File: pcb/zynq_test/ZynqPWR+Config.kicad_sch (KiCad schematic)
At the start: 1 part, among them U1 XC7Z020-2CLG400I

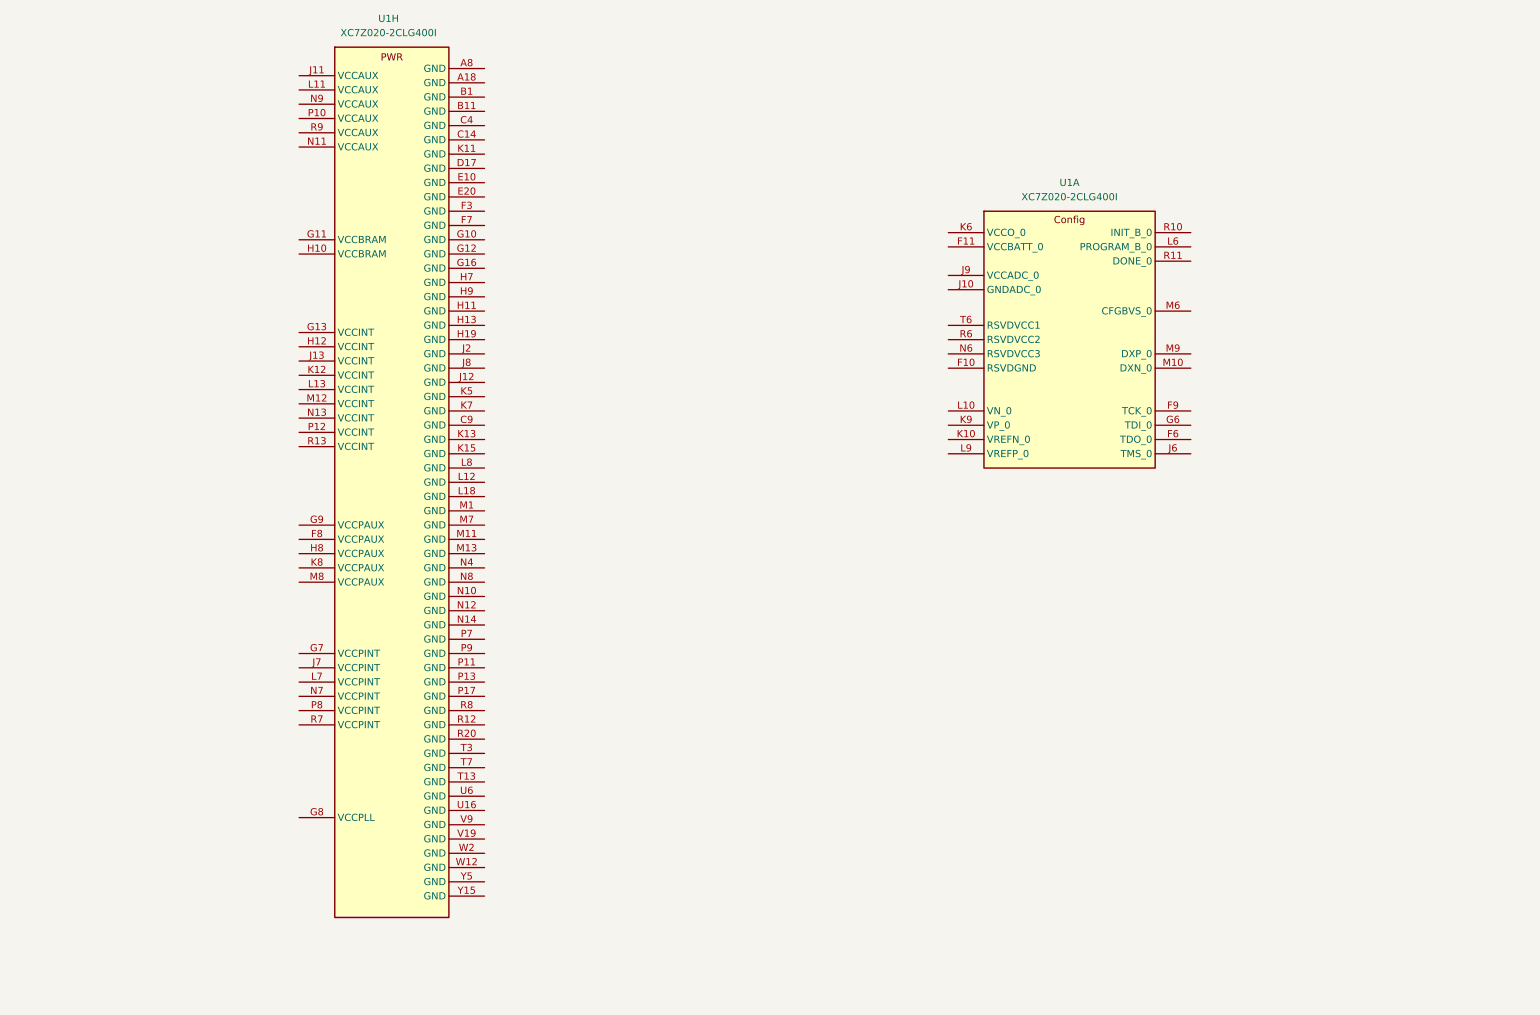
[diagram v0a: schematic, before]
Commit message: Finished PS, started on PWR
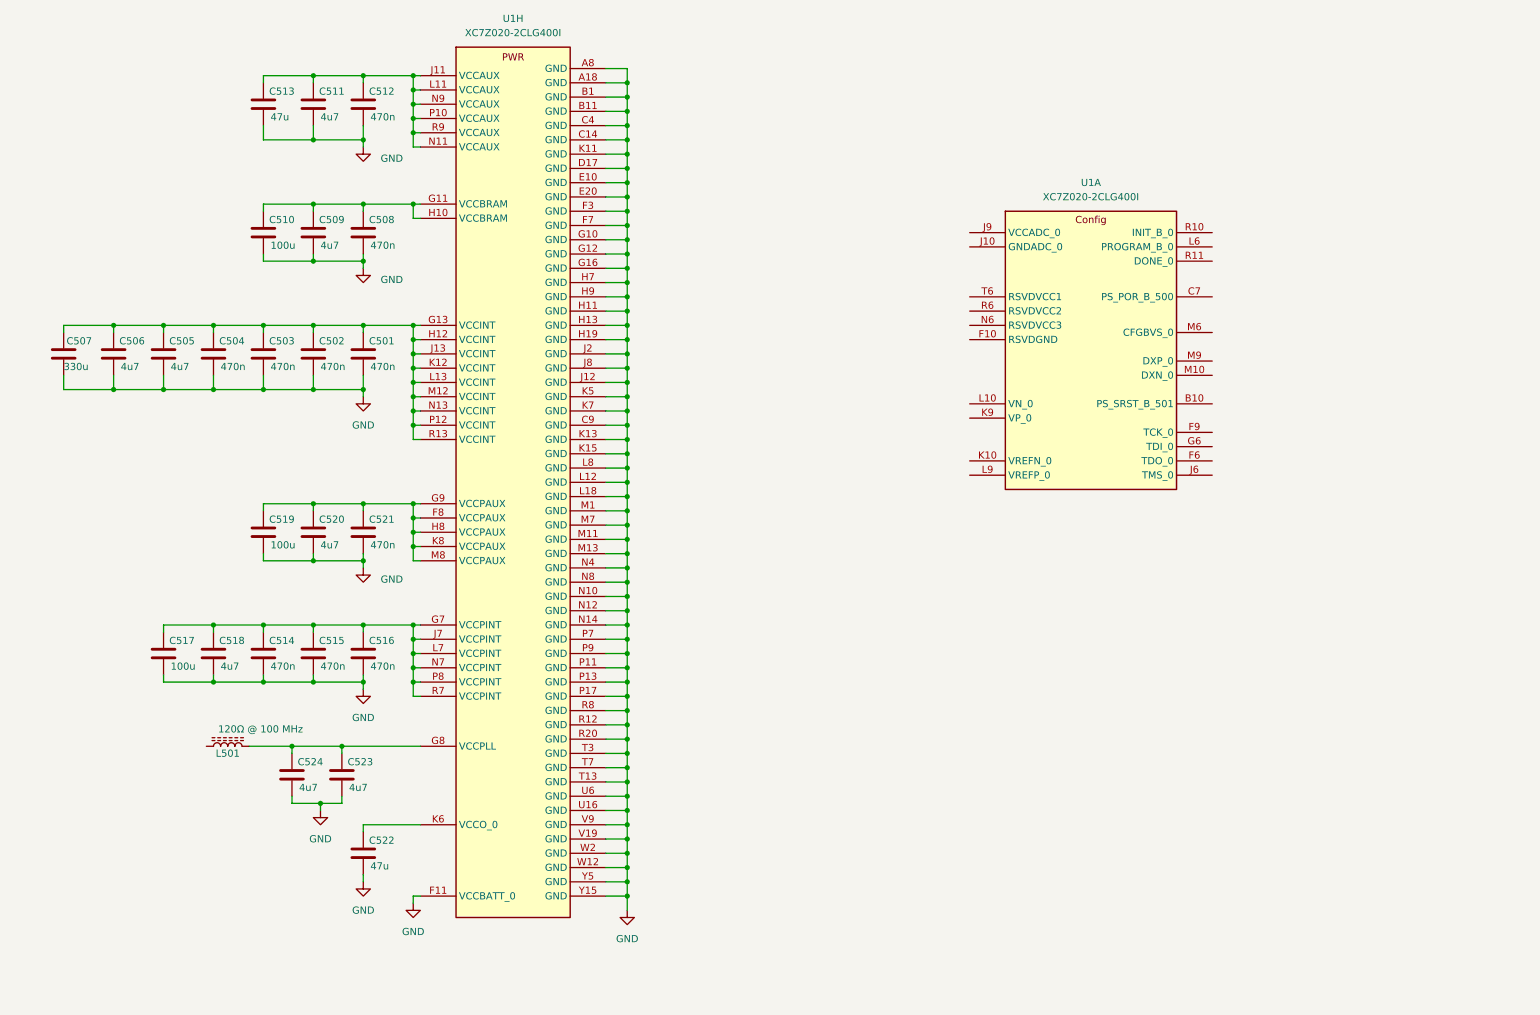
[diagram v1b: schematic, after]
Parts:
- added C501, C502, C503, C504, C508, C512, C514, C515, C516, C521: 470n, symbol Device:C
- added C505, C506, C509, C511, C518, C520, C523, C524: 4u7, symbol Device:C
- added C507: 330u, symbol Device:C
- added C510, C517, C519: 100u, symbol Device:C
- added C513, C522: 47u, symbol Device:C
- added L501: 120Ω @ 100 MHz, symbol Device:L_Ferrite
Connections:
- net GND: now reaches U1.A18 (GND)
- net GND: now also U1.A8 (GND), U1.B1 (GND), U1.B11 (GND), U1.C14 (GND), U1.C4 (GND), U1.C9 (GND), U1.D17 (GND), U1.E10 (GND), U1.E20 (GND), U1.F11 (VCCBATT_0), U1.F3 (GND), U1.F7 (GND), U1.G10 (GND), U1.G12 (GND), U1.G16 (GND), U1.H11 (GND), U1.H13 (GND), U1.H19 (GND), U1.H7 (GND), U1.H9 (GND), U1.J12 (GND), U1.J2 (GND), U1.J8 (GND), U1.K11 (GND), U1.K13 (GND), U1.K15 (GND), U1.K5 (GND), U1.K7 (GND), U1.L12 (GND), U1.L18 (GND), U1.L8 (GND), U1.M1 (GND), U1.M11 (GND), U1.M13 (GND), U1.M7 (GND), U1.N10 (GND), U1.N12 (GND), U1.N14 (GND), U1.N4 (GND), U1.N8 (GND), U1.P11 (GND), U1.P13 (GND), U1.P17 (GND), U1.P7 (GND), U1.P9 (GND), U1.R12 (GND), U1.R20 (GND), U1.R8 (GND), U1.T13 (GND), U1.T3 (GND), U1.T7 (GND), U1.U16 (GND), U1.U6 (GND), U1.V19 (GND), U1.V9 (GND), U1.W12 (GND), U1.W2 (GND), U1.Y15 (GND), U1.Y5 (GND), C501.2, C502.2, C503.2, C504.2, C505.2, C506.2, C507.2, C508.2, C509.2, C510.2, C511.2, C512.2, C513.2, C514.2, C515.2, C516.2, C517.2, C518.2, C519.2, C520.2, C521.2, C522.2, C523.2, C524.2
- net at U1.F8 (VCCPAUX): now also U1.G9 (VCCPAUX), U1.H8 (VCCPAUX), U1.K8 (VCCPAUX), U1.M8 (VCCPAUX), C519.1, C520.1, C521.1
- net at U1.G11 (VCCBRAM): now also U1.H10 (VCCBRAM), C508.1, C509.1, C510.1
- net at U1.G13 (VCCINT): now also U1.H12 (VCCINT), U1.J13 (VCCINT), U1.K12 (VCCINT), U1.L13 (VCCINT), U1.M12 (VCCINT), U1.N13 (VCCINT), U1.P12 (VCCINT), U1.R13 (VCCINT), C501.1, C502.1, C503.1, C504.1, C505.1, C506.1, C507.1
- net at U1.G7 (VCCPINT): now also U1.J7 (VCCPINT), U1.L7 (VCCPINT), U1.N7 (VCCPINT), U1.P8 (VCCPINT), U1.R7 (VCCPINT), C514.1, C515.1, C516.1, C517.1, C518.1
- net at U1.G8 (VCCPLL): now also C523.1, C524.1, L501.2
- net at U1.J11 (VCCAUX): now also U1.L11 (VCCAUX), U1.N11 (VCCAUX), U1.N9 (VCCAUX), U1.P10 (VCCAUX), U1.R9 (VCCAUX), C511.1, C512.1, C513.1
- new net: C522.1, U1.K6 (VCCO_0)
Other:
- moved on the sheet: U1A

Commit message: Finished FPGA decouploing, and jtag programmer
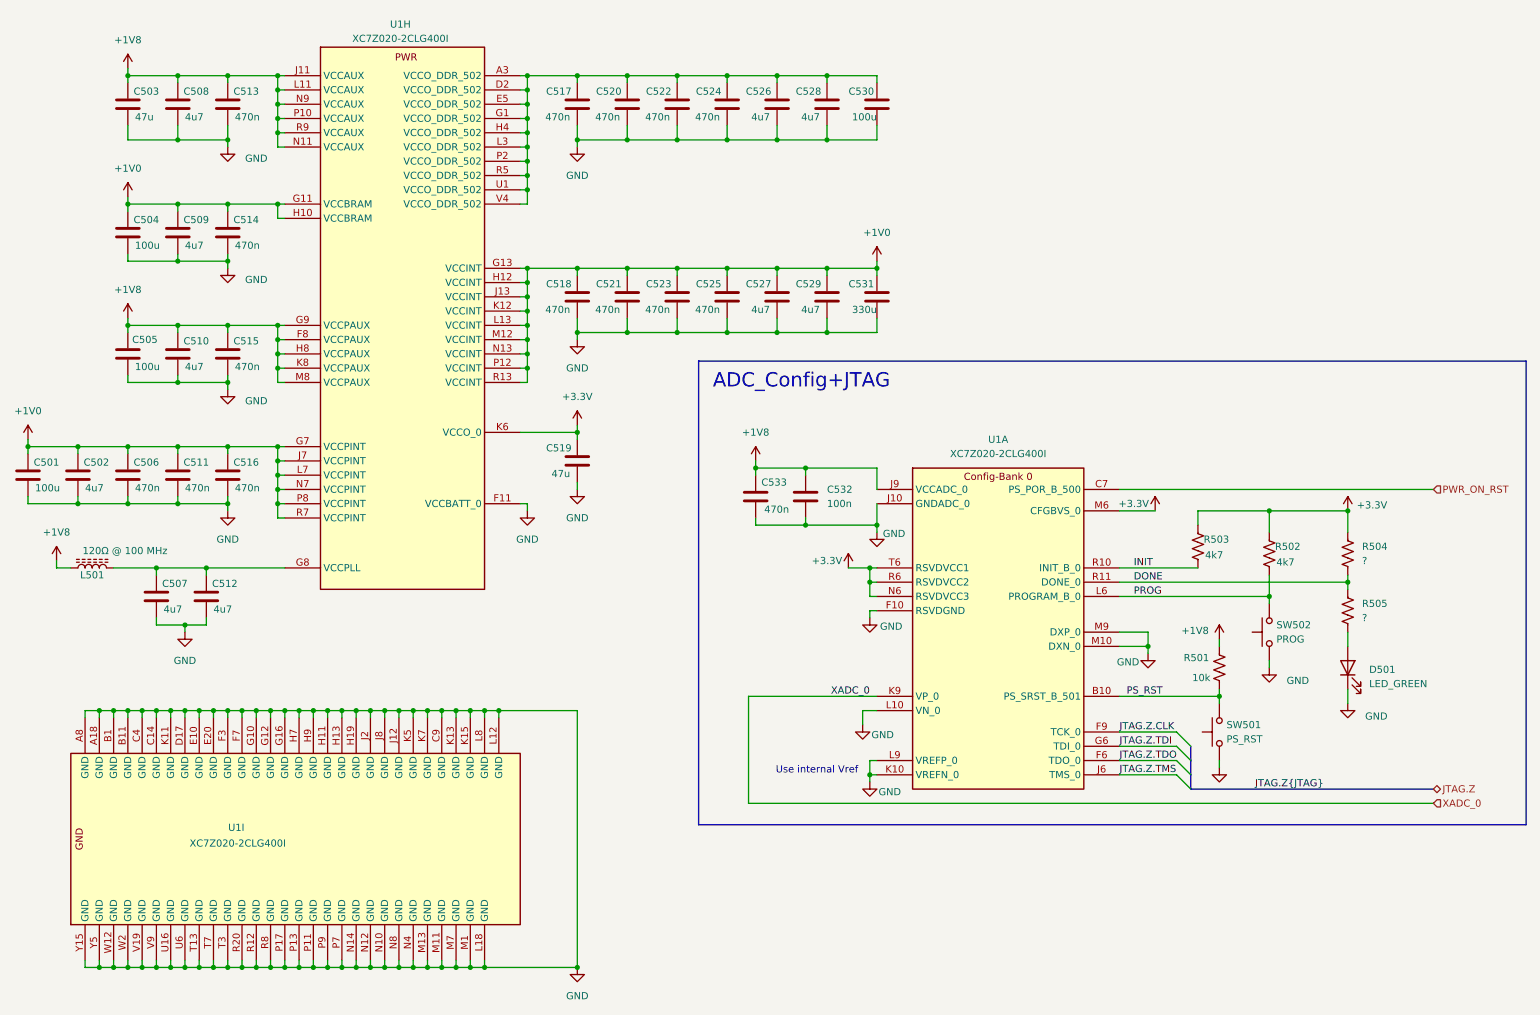
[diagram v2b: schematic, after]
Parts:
- added C517, C520, C522, C524, C533: 470n, symbol Device:C
- added C526, C528: 4u7, symbol Device:C
- added C530: 100u, symbol Device:C
- added C532: 100n, symbol Device:C
- added D501: LED_GREEN, symbol Device:LED
- added R501: 10k, symbol Device:R_US
- added R502, R503: 4k7, symbol Device:R_US
- added R504, R505: ?, symbol Device:R_US
- added SW501: PS_RST, symbol Switch:SW_Push
- added SW502: PROG, symbol Switch:SW_Push
- added unit 9 of U1
- renumbered C517 to C501, C518 to C502, C513 to C503, C510 to C504, C519 to C505, C514 to C506, C524 to C507, C511 to C508, C520 to C510, C515 to C511, C523 to C512, C512 to C513, C508 to C514, C521 to C515, C501 to C518, C522 to C519, C502 to C521, C503 to C523, C504 to C525, C505 to C527, C506 to C529, C507 to C531
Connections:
- net GND: now also U1.F10 (RSVDGND), U1.J10 (GNDADC_0), U1.K10 (VREFN_0), U1.L10 (VN_0), U1.L9 (VREFP_0), U1.M10 (DXN_0), U1.M9 (DXP_0), C517.2, C520.2, C522.2, C524.2, C526.2, C528.2, C530.2, C532.2, C533.2, D501.1 (K), SW501.1, SW502.1, U1.A18 (GND), U1.A8 (GND), U1.B1 (GND), U1.B11 (GND), U1.C14 (GND), U1.C4 (GND), U1.C9 (GND), U1.D17 (GND), U1.E10 (GND), U1.E20 (GND), U1.F3 (GND), U1.F7 (GND), U1.G10 (GND), U1.G12 (GND), U1.G16 (GND), U1.H11 (GND), U1.H13 (GND), U1.H19 (GND), U1.H7 (GND), U1.H9 (GND), U1.J12 (GND), U1.J2 (GND), U1.J8 (GND), U1.K11 (GND), U1.K13 (GND), U1.K15 (GND), U1.K5 (GND), U1.K7 (GND), U1.L12 (GND), U1.L18 (GND), U1.L8 (GND), U1.M1 (GND), U1.M11 (GND), U1.M13 (GND), U1.M7 (GND), U1.N10 (GND), U1.N12 (GND), U1.N14 (GND), U1.N4 (GND), U1.N8 (GND), U1.P11 (GND), U1.P13 (GND), U1.P17 (GND), U1.P7 (GND), U1.P9 (GND), U1.R12 (GND), U1.R20 (GND), U1.R8 (GND), U1.T13 (GND), U1.T3 (GND), U1.T7 (GND), U1.U16 (GND), U1.U6 (GND), U1.V19 (GND), U1.V9 (GND), U1.W12 (GND), U1.W2 (GND), U1.Y15 (GND), U1.Y5 (GND); no longer U1.A18 (GND), U1.A8 (GND), U1.B1 (GND), U1.B11 (GND), U1.C14 (GND), U1.C4 (GND), U1.C9 (GND), U1.D17 (GND), U1.E10 (GND), U1.E20 (GND), U1.F3 (GND), U1.F7 (GND), U1.G10 (GND), U1.G12 (GND), U1.G16 (GND), U1.H11 (GND), U1.H13 (GND), U1.H19 (GND), U1.H7 (GND), U1.H9 (GND), U1.J12 (GND), U1.J2 (GND), U1.J8 (GND), U1.K11 (GND), U1.K13 (GND), U1.K15 (GND), U1.K5 (GND), U1.K7 (GND), U1.L12 (GND), U1.L18 (GND), U1.L8 (GND), U1.M1 (GND), U1.M11 (GND), U1.M13 (GND), U1.M7 (GND), U1.N10 (GND), U1.N12 (GND), U1.N14 (GND), U1.N4 (GND), U1.N8 (GND), U1.P11 (GND), U1.P13 (GND), U1.P17 (GND), U1.P7 (GND), U1.P9 (GND), U1.R12 (GND), U1.R20 (GND), U1.R8 (GND), U1.T13 (GND), U1.T3 (GND), U1.T7 (GND), U1.U16 (GND), U1.U6 (GND), U1.V19 (GND), U1.V9 (GND), U1.W12 (GND), U1.W2 (GND), U1.Y15 (GND), U1.Y5 (GND)
- net +1V8: now reaches C505.1, C510.1, C515.1, U1.F8 (VCCPAUX), U1.G9 (VCCPAUX), U1.H8 (VCCPAUX), U1.K8 (VCCPAUX), U1.M8 (VCCPAUX)
- net +1V8: now also C503.1, C508.1, C513.1, L501.1, U1.J11 (VCCAUX), U1.J9 (VCCADC_0), U1.L11 (VCCAUX), U1.N11 (VCCAUX), U1.N9 (VCCAUX), U1.P10 (VCCAUX), U1.R9 (VCCAUX), C532.1, C533.1, R501.1
- net +1V0: now reaches C501.1, C502.1, C506.1, C511.1, C516.1, U1.G7 (VCCPINT), U1.J7 (VCCPINT), U1.L7 (VCCPINT), U1.N7 (VCCPINT), U1.P8 (VCCPINT), U1.R7 (VCCPINT)
- net +1V0: now also C504.1, C509.1, C514.1, C518.1, C521.1, C523.1, C525.1, C527.1, C529.1, C531.1, U1.G11 (VCCBRAM), U1.G13 (VCCINT), U1.H10 (VCCBRAM), U1.H12 (VCCINT), U1.J13 (VCCINT), U1.K12 (VCCINT), U1.L13 (VCCINT), U1.M12 (VCCINT), U1.N13 (VCCINT), U1.P12 (VCCINT), U1.R13 (VCCINT)
- net +3.3V: now reaches C519.1, U1.K6 (VCCO_0)
- net +3.3V: now also U1.M6 (CFGBVS_0), U1.N6 (RSVDVCC3), U1.R6 (RSVDVCC2), U1.T6 (RSVDVCC1), R502.1, R503.1, R504.1
- net PS_RST: now reaches U1.B10 (PS_SRST_B_501)
- net PS_RST: now also R501.2, SW501.2
- net PWR_ON_RST: now reaches U1.C7 (PS_POR_B_500)
- net JTAG.Z.TDO: now reaches U1.F6 (TDO_0)
- net JTAG.Z.CLK: now reaches U1.F9 (TCK_0)
- net JTAG.Z.TDI: now reaches U1.G6 (TDI_0)
- net JTAG.Z.TMS: now reaches U1.J6 (TMS_0)
- net XADC_0: now reaches U1.K9 (VP_0)
- net PROG: now reaches U1.L6 (PROGRAM_B_0)
- net PROG: now also R502.2, SW502.2
- net INIT: now reaches U1.R10 (INIT_B_0)
- net INIT: now also R503.2
- net DONE: now reaches U1.R11 (DONE_0)
- net DONE: now also R504.2, R505.1
- new net: D501.2 (A), R505.2
- new net: C517.1, C520.1, C522.1, C524.1, C526.1, C528.1, C530.1, U1.A3 (VCCO_DDR_502), U1.D2 (VCCO_DDR_502), U1.E5 (VCCO_DDR_502), U1.G1 (VCCO_DDR_502), U1.H4 (VCCO_DDR_502), U1.L3 (VCCO_DDR_502), U1.P2 (VCCO_DDR_502), U1.R5 (VCCO_DDR_502), U1.U1 (VCCO_DDR_502), U1.V4 (VCCO_DDR_502)
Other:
- note added: "ADC_Config+JTAG"
- note added: "Use internal Vref"
- moved on the sheet: C501, C502, C503, C504, C505, C506, C507, C508, C509, C510, C511, C512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

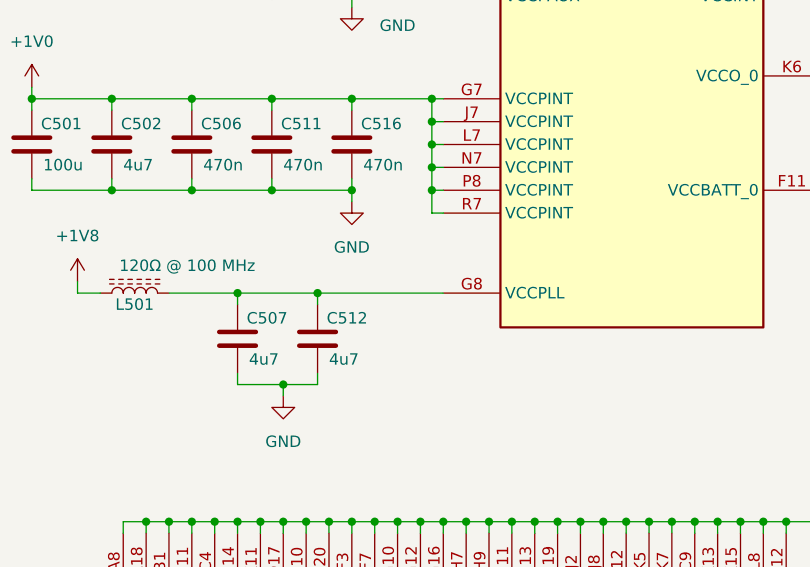
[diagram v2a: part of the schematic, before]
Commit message: Finished Ethernet, swapped FTDI chip for QFN
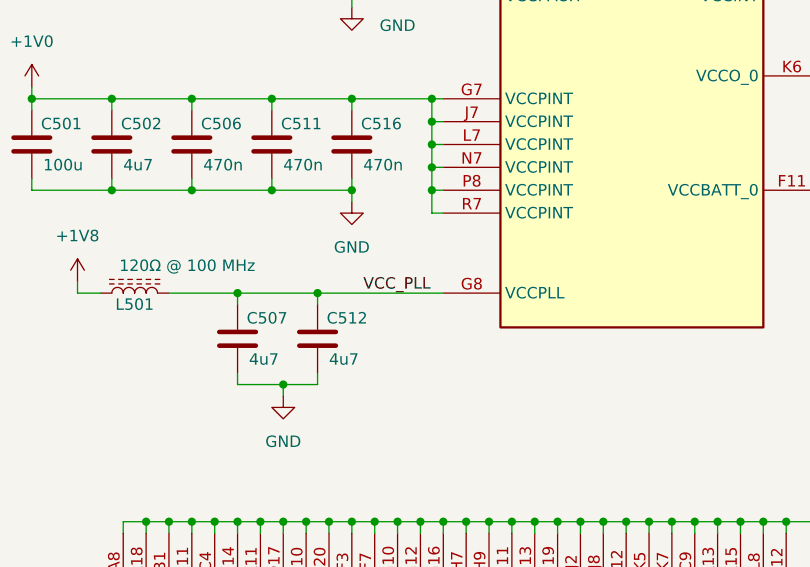
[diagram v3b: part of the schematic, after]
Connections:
- net VCC_PLL: now reaches C507.1, C512.1, L501.2, U1.G8 (VCCPLL)
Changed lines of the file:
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@@
 		(at 251.46 120.65)
 		(diameter 0)
-		(color 0 0 194 1)
+		(color 0 0 0 0)
 	)
 	(junction
@@
 			(width 0)
 			(type default)
-			(color 0 0 194 1)
 		)
 	)
@@
 			(width 0)
 			(type default)
-			(color 0 0 194 1)
 		)
 	)
@@
 			(width 0)
 			(type default)
-			(color 0 0 194 1)
 		)
 	)
@@
 		(effects
 			(font
+				(size 1.27 1.27)
+			)
+			(justify left bottom)
+		)
+	)
+	(label "VCC_PLL"
+		(at 53.34 118.11 0)
+		(effects
+			(font

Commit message: Finished HDMI
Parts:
- U1: footprint Zynq:CLG400_ZYNQ-7000_AMD -> Package_BGA:Xilinx_CLG400
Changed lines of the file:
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@@
 			)
 		)
-		(property "Footprint" "Zynq:CLG400_ZYNQ-7000_AMD"
+		(property "Footprint" "Package_BGA:Xilinx_CLG400"
 			(at 54.61 27.94 0)
 			(effects
@@
 			)
 		)
-		(property "Footprint" "Zynq:CLG400_ZYNQ-7000_AMD"
+		(property "Footprint" "Package_BGA:Xilinx_CLG400"
 			(at 160.02 53.34 0)
 			(effects
@@
 			)
 		)
-		(property "Footprint" "Zynq:CLG400_ZYNQ-7000_AMD"
+		(property "Footprint" "Package_BGA:Xilinx_CLG400"
 			(at -22.86 195.58 0)
 			(effects
